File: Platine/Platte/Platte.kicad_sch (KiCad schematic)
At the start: 20 parts, among them J1 Conn_01x07_MountingPin, J3 Conn_01x04_Socket

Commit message: Small correction. Everything finished
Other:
- note added: "Outputs: fil_da1, fil_da2, fil_da3"
- note removed: "Outputs:"
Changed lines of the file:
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@@
 		)
 	)
-	(text "Outputs: "
+	(text "Outputs: fil_da1, \nfil_da2, fil_da3"
 		(exclude_from_sim no)
-		(at 46.482 101.854 0)
+		(at 38.354 103.632 0)
 		(effects
 			(font

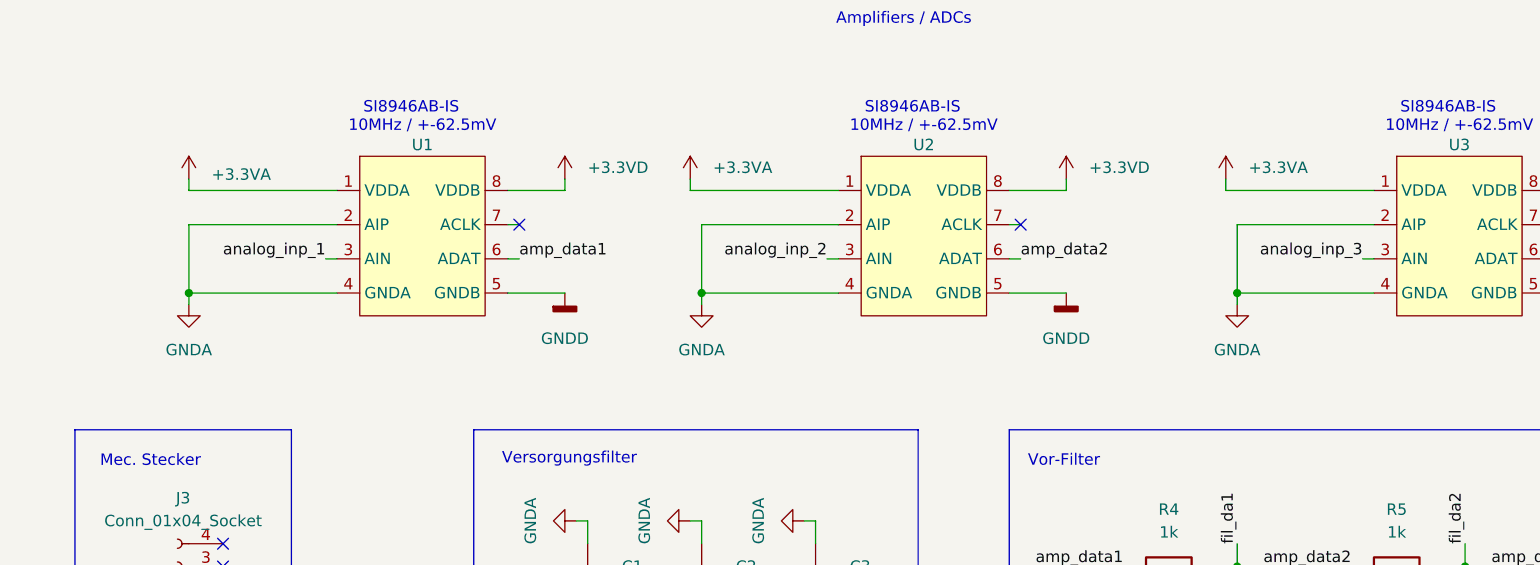
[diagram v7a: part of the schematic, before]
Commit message: corrections on platte PCB
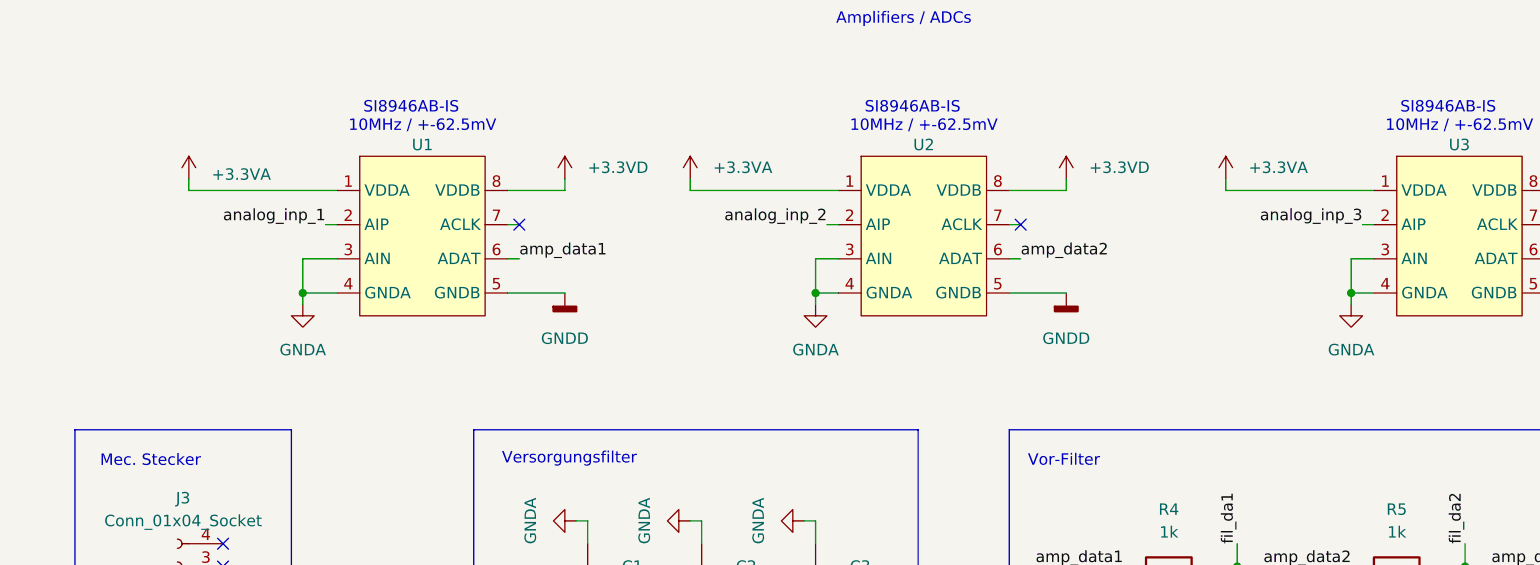
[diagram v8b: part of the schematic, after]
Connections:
- net GNDA: now also U1.3 (AIN), U2.3 (AIN), U3.3 (AIN); no longer U1.2 (AIP), U2.2 (AIP), U3.2 (AIP)
- net analog_inp_1: now also U1.2 (AIP); no longer U1.3 (AIN)
- net analog_inp_2: now also U2.2 (AIP); no longer U2.3 (AIN)
- net analog_inp_3: now also U3.2 (AIP); no longer U3.3 (AIN)
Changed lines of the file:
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@@
 	(paper "A4")
 	(junction
-		(at 139.7 49.53)
+		(at 199.39 80.01)
 		(diameter 0)
 		(color 0 0 0 0)
 	)
 	(junction
-		(at 199.39 80.01)
+		(at 95.25 49.53)
 		(diameter 0)
 		(color 0 0 0 0)
@@
 	)
 	(junction
-		(at 250.19 80.01)
+		(at 152.4 49.53)
 		(diameter 0)
 		(color 0 0 0 0)
 	)
 	(junction
-		(at 82.55 49.53)
+		(at 250.19 80.01)
 		(diameter 0)
 		(color 0 0 0 0)
 	)
 	(junction
-		(at 224.79 80.01)
+		(at 212.09 49.53)
 		(diameter 0)
 		(color 0 0 0 0)
 	)
 	(junction
-		(at 35.56 25.4)
+		(at 224.79 80.01)
 		(diameter 0)
 		(color 0 0 0 0)
 	)
 	(junction
-		(at 199.39 49.53)
+		(at 35.56 25.4)
 		(diameter 0)
 		(color 0 0 0 0)
@@
 	(wire
 		(pts
-			(xy 139.7 41.91) (xy 139.7 49.53)
+			(xy 212.09 45.72) (xy 212.09 49.53)
 		)
 		(stroke
@@
 	(wire
 		(pts
-			(xy 154.94 41.91) (xy 139.7 41.91)
+			(xy 139.7 96.52) (xy 138.43 96.52)
 		)
 		(stroke
@@
 	(wire
 		(pts
-			(xy 82.55 41.91) (xy 82.55 49.53)
+			(xy 186.69 80.01) (xy 187.96 80.01)
 		)
 		(stroke
@@
 	(wire
 		(pts
-			(xy 139.7 96.52) (xy 138.43 96.52)
+			(xy 127 90.17) (xy 127 85.09)
 		)
 		(stroke
@@
 	(wire
 		(pts
-			(xy 186.69 80.01) (xy 187.96 80.01)
+			(xy 29.21 90.17) (xy 36.83 90.17)
 		)
 		(stroke
@@
 	(wire
 		(pts
-			(xy 127 90.17) (xy 127 85.09)
+			(xy 20.32 25.4) (xy 20.32 31.75)
 		)
 		(stroke
@@
 	(wire
 		(pts
-			(xy 29.21 90.17) (xy 36.83 90.17)
+			(xy 127 90.17) (xy 139.7 90.17)
+		)
+		(stroke
+			(width 0)
+			(type default)
+		)
+	)
+	(polyline
+		(pts
+			(xy 16.51 17.78) (xy 16.51 49.53)
 		)
 		(stroke
@@
 	(wire
 		(pts
-			(xy 20.32 25.4) (xy 20.32 31.75)
+			(xy 35.56 39.37) (xy 35.56 41.91)
 		)
 		(stroke
@@
 	(wire
 		(pts
-			(xy 127 90.17) (xy 139.7 90.17)
+			(xy 153.67 41.91) (xy 154.94 41.91)
 		)
 		(stroke
@@
 		)
 	)
-	(polyline
+	(wire
 		(pts
-			(xy 16.51 17.78) (xy 16.51 49.53)
+			(xy 214.63 45.72) (xy 212.09 45.72)
 		)
 		(stroke
@@
 	(wire
 		(pts
-			(xy 35.56 39.37) (xy 35.56 41.91)
+			(xy 29.21 87.63) (xy 30.48 87.63)
 		)
 		(stroke
@@
 	(wire
 		(pts
-			(xy 97.79 45.72) (xy 99.06 45.72)
+			(xy 152.4 96.52) (xy 151.13 96.52)
 		)
 		(stroke
@@
 	(wire
 		(pts
-			(xy 29.21 87.63) (xy 30.48 87.63)
+			(xy 212.09 49.53) (xy 214.63 49.53)
 		)
 		(stroke
@@
 	(wire
 		(pts
-			(xy 152.4 96.52) (xy 151.13 96.52)
+			(xy 27.94 25.4) (xy 35.56 25.4)
 		)
 		(stroke
@@
 	(wire
 		(pts
-			(xy 199.39 49.53) (xy 214.63 49.53)
+			(xy 224.79 90.17) (xy 224.79 92.71)
 		)
 		(stroke
@@
 	(wire
 		(pts
-			(xy 27.94 25.4) (xy 35.56 25.4)
+			(xy 213.36 41.91) (xy 214.63 41.91)
 		)
 		(stroke
@@
 	(wire
 		(pts
-			(xy 224.79 90.17) (xy 224.79 92.71)
+			(xy 152.4 49.53) (xy 154.94 49.53)
 		)
 		(stroke
@@
 	(wire
 		(pts
-			(xy 139.7 49.53) (xy 154.94 49.53)
+			(xy 154.94 45.72) (xy 152.4 45.72)
 		)
 		(stroke
@@
 	(wire
 		(pts
-			(xy 213.36 45.72) (xy 214.63 45.72)
+			(xy 138.43 38.1) (xy 154.94 38.1)
 		)
 		(stroke
@@
 	(wire
 		(pts
-			(xy 138.43 38.1) (xy 154.94 38.1)
+			(xy 127 96.52) (xy 125.73 96.52)
 		)
 		(stroke
@@
 	(wire
 		(pts
-			(xy 127 96.52) (xy 125.73 96.52)
+			(xy 99.06 45.72) (xy 95.25 45.72)
 		)
 		(stroke
@@
 	(wire
 		(pts
-			(xy 82.55 49.53) (xy 82.55 50.8)
+			(xy 95.25 49.53) (xy 95.25 50.8)
 		)
 		(stroke
@@
 	(wire
 		(pts
-			(xy 153.67 45.72) (xy 154.94 45.72)
-		)
-		(stroke
-			(width 0)
-			(type default)
-		)
-	)
-	(wire
-		(pts
 			(xy 224.79 77.47) (xy 224.79 80.01)
 		)
@@
 		)
 	)
+	(wire
+		(pts
+			(xy 97.79 41.91) (xy 99.06 41.91)
+		)
+		(stroke
+			(width 0)
+			(type default)
+		)
+	)
 	(polyline
 		(pts
@@
 	(wire
 		(pts
-			(xy 99.06 41.91) (xy 82.55 41.91)
+			(xy 95.25 49.53) (xy 99.06 49.53)
 		)
 		(stroke
@@
 	(wire
 		(pts
-			(xy 82.55 49.53) (xy 99.06 49.53)
+			(xy 138.43 36.83) (xy 138.43 38.1)
 		)
 		(stroke
@@
 	(wire
 		(pts
-			(xy 138.43 36.83) (xy 138.43 38.1)
+			(xy 152.4 49.53) (xy 152.4 50.8)
 		)
 		(stroke
@@
 	(wire
 		(pts
-			(xy 139.7 49.53) (xy 139.7 50.8)
+			(xy 95.25 45.72) (xy 95.25 49.53)
 		)
 		(stroke
@@
 	(wire
 		(pts
-			(xy 199.39 49.53) (xy 199.39 50.8)
+			(xy 212.09 49.53) (xy 212.09 50.8)
 		)
 		(stroke
@@
 	(wire
 		(pts
+			(xy 152.4 45.72) (xy 152.4 49.53)
+		)
+		(stroke
+			(width 0)
+			(type default)
+		)
+	)
+	(wire
+		(pts
 			(xy 127 74.93) (xy 127 77.47)
 		)
@@
 	(wire
 		(pts
-			(xy 199.39 41.91) (xy 199.39 49.53)
-		)
-		(stroke
-			(width 0)
-			(type default)
-		)
-	)
-	(wire
-		(pts
 			(xy 250.19 77.47) (xy 250.19 80.01)
 		)
@@
 	(wire
 		(pts
-			(xy 214.63 41.91) (xy 199.39 41.91)
-		)
-		(stroke
-			(width 0)
-			(type default)
-		)
-	)
-	(wire
-		(pts
 			(xy 250.19 90.17) (xy 250.19 92.71)
 		)
@@
 	)
 	(label "analog_inp_3"
-		(at 213.36 45.72 180)
+		(at 213.36 41.91 180)
 		(fields_autoplaced yes)
 		(effects
@@
 	)
 	(label "analog_inp_2"
-		(at 153.67 45.72 180)
+		(at 153.67 41.91 180)
 		(fields_autoplaced yes)
 		(effects
@@
 	)
 	(label "analog_inp_1"
-		(at 97.79 45.72 180)
+		(at 97.79 41.91 180)
 		(fields_autoplaced yes)
 		(effects
@@
 	(symbol
 		(lib_id "power:GNDA")
-		(at 199.39 50.8 0)
+		(at 212.09 50.8 0)
 		(unit 1)
 		(exclude_from_sim no)
@@
 		(fields_autoplaced yes)
 		(property "Reference" "#PWR017"
-			(at 199.39 57.15 0)
+			(at 212.09 57.15 0)
 			(effects
 				(font
@@
 		)
 		(property "Value" "GNDA"
-			(at 199.39 55.88 0)
+			(at 212.09 55.88 0)
 			(effects
 				(font
@@
 		)
 		(property "Footprint" ""
-			(at 199.39 50.8 0)
+			(at 212.09 50.8 0)
 			(effects
 				(font
@@
 		)
 		(property "Datasheet" ""
-			(at 199.39 50.8 0)
+			(at 212.09 50.8 0)
 			(effects
 				(font
@@
 		)
 		(property "Description" ""
-			(at 199.39 50.8 0)
+			(at 212.09 50.8 0)
 			(effects
 				(font
@@
 	(symbol
 		(lib_id "power:GNDA")
-		(at 82.55 50.8 0)
+		(at 95.25 50.8 0)
 		(unit 1)
 		(exclude_from_sim no)
@@
 		(fields_autoplaced yes)
 		(property "Reference" "#PWR010"
-			(at 82.55 57.15 0)
+			(at 95.25 57.15 0)
 			(effects
 				(font
@@
 		)
 		(property "Value" "GNDA"
-			(at 82.55 55.88 0)
+			(at 95.25 55.88 0)
 			(effects
 				(font
@@
 		)
 		(property "Footprint" ""
-			(at 82.55 50.8 0)
+			(at 95.25 50.8 0)
 			(effects
 				(font
@@
 		)
 		(property "Datasheet" ""
-			(at 82.55 50.8 0)
+			(at 95.25 50.8 0)
 			(effects
 				(font
@@
 		)
 		(property "Description" ""
-			(at 82.55 50.8 0)
+			(at 95.25 50.8 0)
 			(effects
 				(font
@@
 	(symbol
 		(lib_id "power:GNDA")
-		(at 139.7 50.8 0)
+		(at 152.4 50.8 0)
 		(unit 1)
 		(exclude_from_sim no)
@@
 		(fields_autoplaced yes)
 		(property "Reference" "#PWR08"
-			(at 139.7 57.15 0)
+			(at 152.4 57.15 0)
 			(effects
 				(font
@@
 		)
 		(property "Value" "GNDA"
-			(at 139.7 55.88 0)
+			(at 152.4 55.88 0)
 			(effects
 				(font
@@
 		)
 		(property "Footprint" ""
-			(at 139.7 50.8 0)
+			(at 152.4 50.8 0)
 			(effects
 				(font
@@
 		)
 		(property "Datasheet" ""
-			(at 139.7 50.8 0)
+			(at 152.4 50.8 0)
 			(effects
 				(font
@@
 		)
 		(property "Description" ""
-			(at 139.7 50.8 0)
+			(at 152.4 50.8 0)
 			(effects
 				(font
